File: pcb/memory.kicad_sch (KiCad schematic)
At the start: 3 parts, among them U6 MT41K256M16TW-107:P TR, U7 MX25L12835F

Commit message: vref
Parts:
- added C69, C71, C72, C73: 0.1uF, Capacitor_SMD:C_0402_1005Metric, symbol library:C
- added C70: 4.7uF, Capacitor_SMD:C_0603_1608Metric, symbol library:C
- added R31, R32: 2.2K 1%, Resistor_SMD:R_0402_1005Metric, symbol library:R_US
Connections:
- net 1V35_DDR: now also C71.2, C72.2, C73.2, R31.1
- net GND: now also C69.1, C70.2, C71.1, C72.1, C73.1, R32.2
- net at U6.H1 (V_{REFDQ}): now also U6.M8 (V_{REFCA}), C69.2, C70.1, R31.2, R32.1
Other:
- moved on the sheet: R20, U6, U7

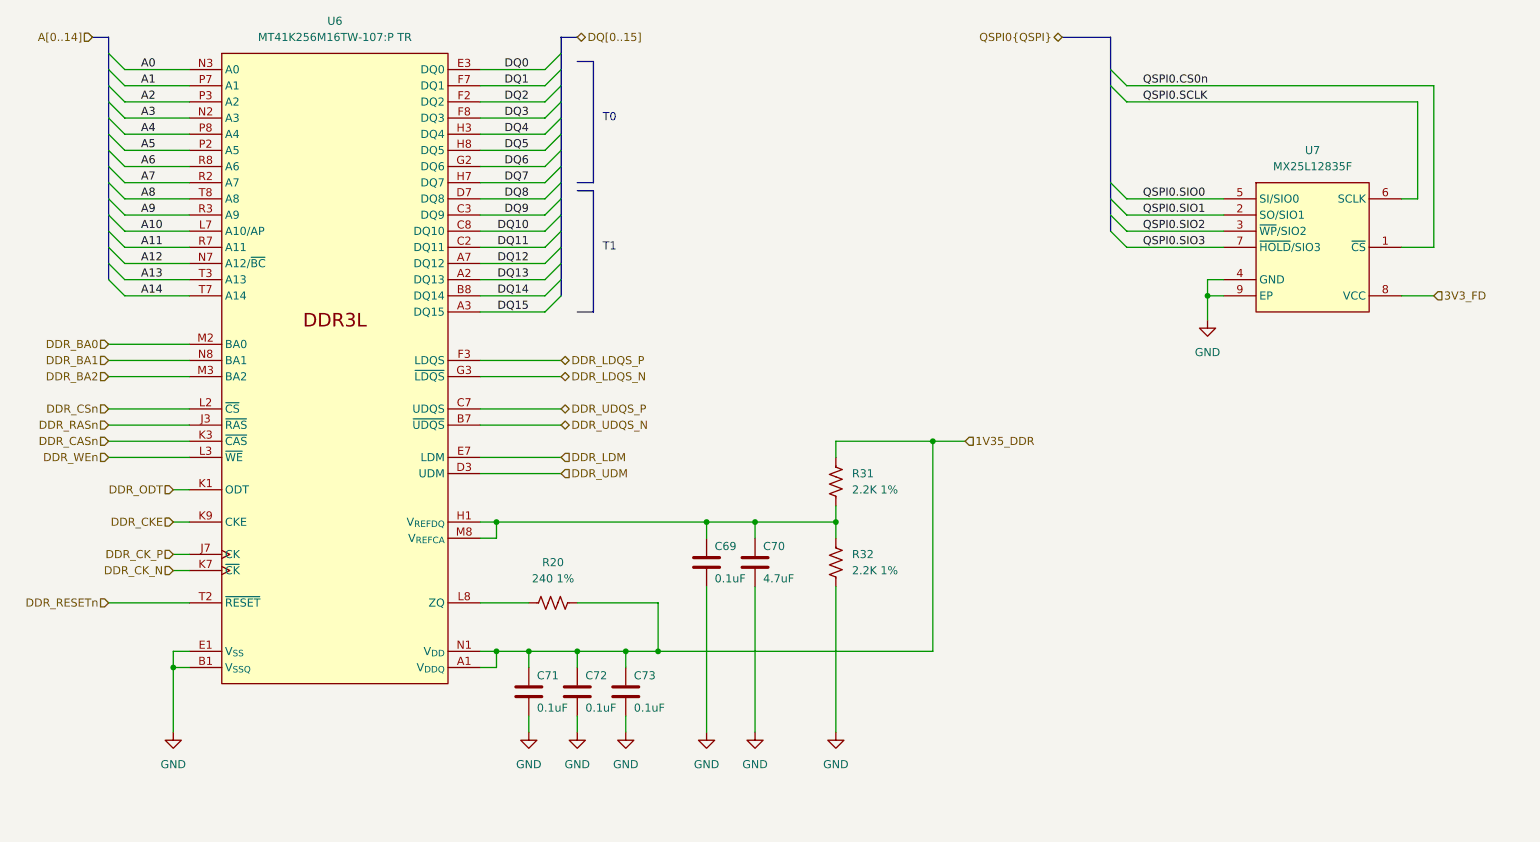
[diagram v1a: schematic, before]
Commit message: change to 8 layers, impedance calc, ddr routing
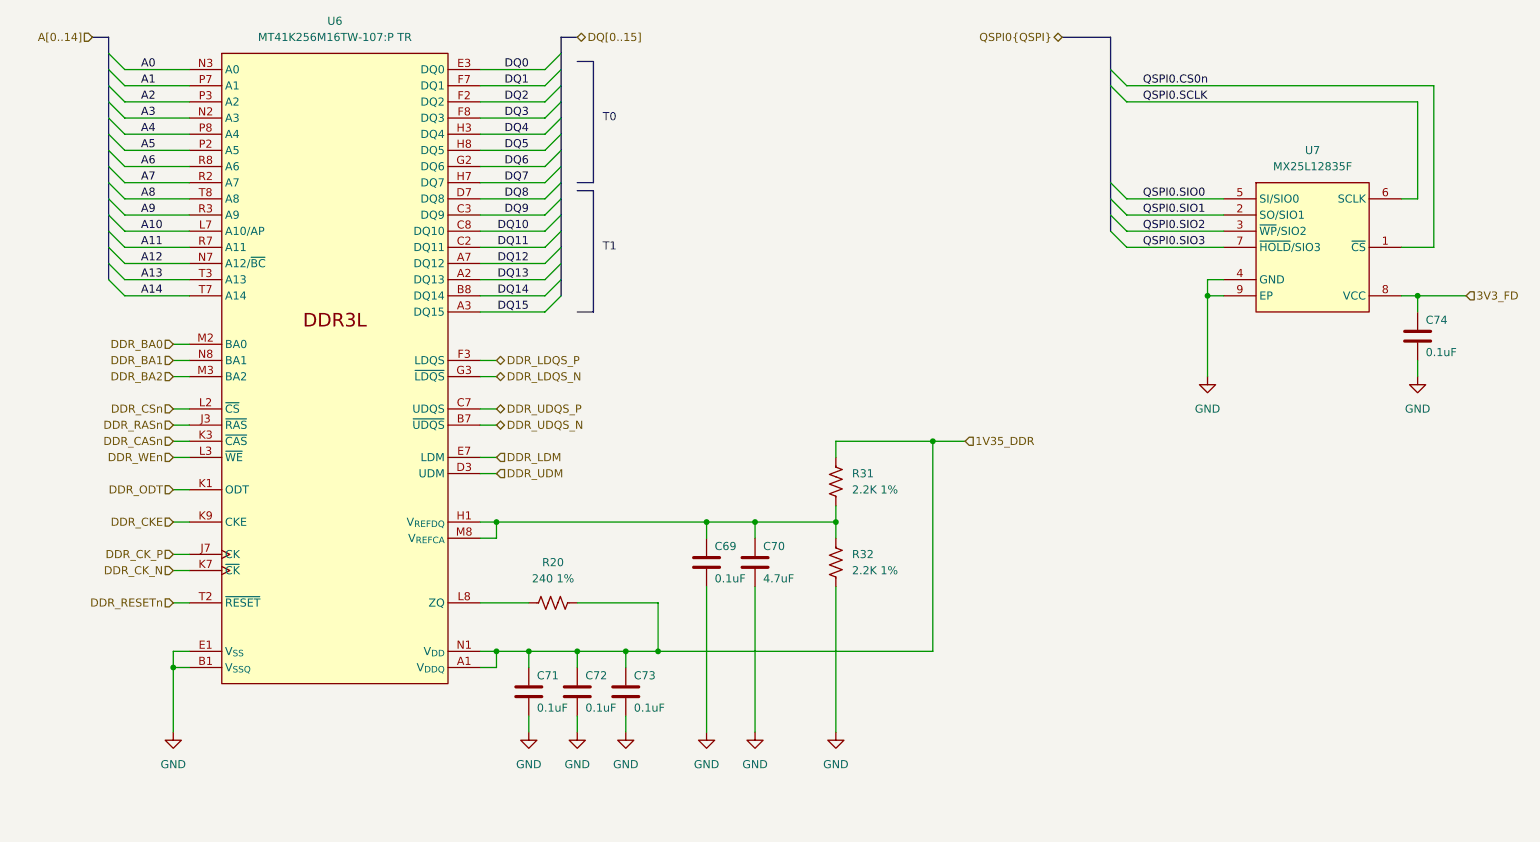
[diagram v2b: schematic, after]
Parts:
- added C74: 0.1uF, Capacitor_SMD:C_0402_1005Metric, symbol library:C
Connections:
- net 3V3_FD: now also C74.2
- net GND: now also C74.1
